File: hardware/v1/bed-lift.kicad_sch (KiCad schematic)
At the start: 69 parts, among them J1 SM04B-SRSS-TB, J2 S2P-VH, J3 SM04B-SRSS-TB, J4 S3B-XH-A, J5 S6B-XH-A, J6 Conn_02x08_Odd_Even, J7 S6B-XH-A, J8 BM04B-SRSS-TB, J9 Conn_ST_STDC14, Q1 MMBT3904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

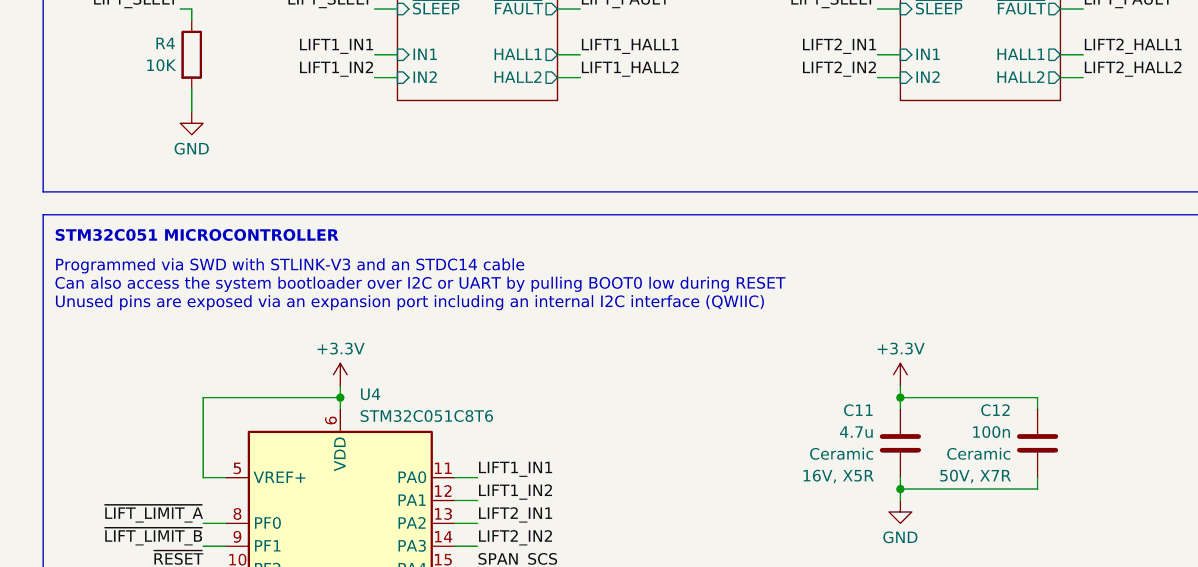
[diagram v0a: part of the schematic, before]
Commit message: Correct the BOOT0 pin polarity in the documentation.
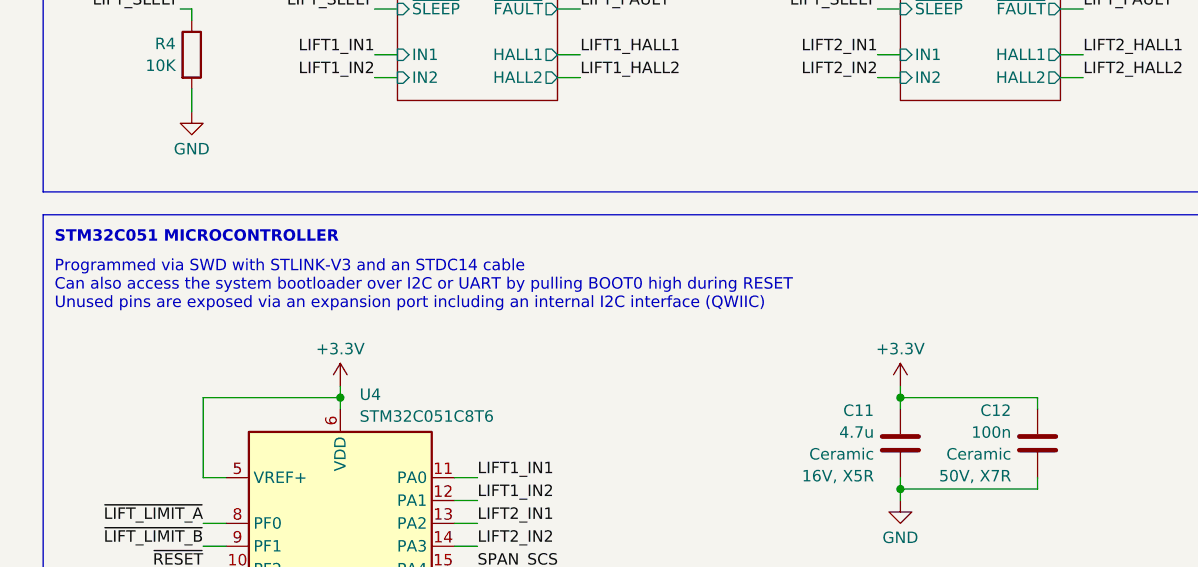
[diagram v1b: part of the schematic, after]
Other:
- note added: "Programmed via SWD with STLINK-V3 and an STDC14 cable Can also access the system bootloader over I2C or UART by pulling BOOT0 high during RESET Unused pins are exposed via an expansion port including an internal I2C interface (QWIIC)"
- note removed: "Programmed via SWD with STLINK-V3 and an STDC14 cable Can also access the system bootloader over I2C or UART by pulling BOOT0 low during RESET Unused pins are exposed via an expansion port including an internal I2C interface (QWIIC)"
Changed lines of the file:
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@@
 		)
 	)
-	(text "Programmed via SWD with STLINK-V3 and an STDC14 cable\nCan also access the system bootloader over I2C or UART by pulling BOOT0 low during RESET\nUnused pins are exposed via an expansion port including an internal I2C interface (QWIIC)"
+	(text "Programmed via SWD with STLINK-V3 and an STDC14 cable\nCan also access the system bootloader over I2C or UART by pulling BOOT0 high during RESET\nUnused pins are exposed via an expansion port including an internal I2C interface (QWIIC)"
 		(exclude_from_sim no)
 		(at 15.24 107.95 0)

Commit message: Finalize for production of v1.0 revision.
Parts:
- BZ1: now fitted; now in the parts list
- C3: Alternative A750KW687M1EAAE016 -> (none); Part Alternative (none) -> A750KW687M1EAAE016
- D1: FT Rotation Offset 180 -> 0
- D2, D3: value PESD5V0S2UAT -> PESD5V0L2UU; footprint Package_TO_SOT_SMD:SOT-23 -> Package_TO_SOT_SMD:SOT-323_SC-70; FT Rotation Offset (none) -> 180; LCSC C552572 -> C78769; LCSC Alternative (none) -> C28646364
- D5: LCSC Alternative (none) -> C456091; LCSC_Alternative C456091 -> (none)
- J1, J3: Alternative GT-A1002WRS-104SBT01 -> (none); LCSC Alternative (none) -> C41431904; LCSC_Alternative C41431904 -> (none); Part Alternative (none) -> GT-A1002WRS-104SBT01
- Q1: LCSC Alternative (none) -> C239187; LCSC_Alternative C239187 -> (none)
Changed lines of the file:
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@@
 		(unit 1)
 		(exclude_from_sim no)
-		(in_bom no)
+		(in_bom yes)
 		(on_board yes)
-		(dnp yes)
+		(dnp no)
 		(fields_autoplaced yes)
 		(property "Reference" "BZ1"
@@
 	)
 	(symbol
+		(lib_id "Device:D_Zener_Dual_CommonAnode_KKA_Parallel")
+		(at 222.25 142.24 0)
+		(mirror y)
+		(unit 1)
+		(exclude_from_sim no)
+		(in_bom yes)
+		(on_board yes)
+		(dnp no)
+		(property "Reference" "D2"
+			(at 229.87 141.0857 0)
+			(effects
+				(font
+					(size 1.27 1.27)
+				)
+				(justify right)
+			)
+		)
+		(property "Value" "PESD5V0L2UU"
+			(at 229.87 143.51 0)
+			(effects
+				(font
+					(size 1.27 1.27)
+				)
+				(justify right)
+			)
+		)
+		(property "Footprint" "Package_TO_SOT_SMD:SOT-323_SC-70"
+			(at 223.52 142.24 0)
+			(effects
+				(font
+					(size 1.27 1.27)
+				)
+				(hide yes)
+			)
+		)
+		(property "Datasheet" "https://assets.nexperia.com/documents/data-sheet/PESD5V0L2UU.pdf"
+			(at 223.52 142.24 0)
+			(effects
+				(font
+					(size 1.27 1.27)
+				)
+				(hide yes)
+			)
+		)
+		(property "Description" "Dual Zener diode, common anode on pin 3"
+			(at 222.25 142.24 0)
+			(effects
+				(font
+					(size 1.27 1.27)
+				)
+				(hide yes)
+			)
+		)
+		(property "LCSC" "C78769"
+			(at 222.25 142.24 0)
+			(effects
+				(font
+					(size 1.27 1.27)
+				)
+				(hide yes)
+			)
+		)
+		(property "LCSC Alternative" "C28646364"
+			(at 222.25 142.24 0)
+			(effects
+				(font
+					(size 1.27 1.27)
+				)
+				(hide yes)
+			)
+		)
+		(property "FT Rotation Offset" "180"
+			(at 222.25 142.24 0)
+			(effects
+				(font
+					(size 1.27 1.27)
+				)
+				(hide yes)
+			)
+		)
+		(pin "2"
+		)
+		(pin "3"
+		)
+		(pin "1"
+		)
+		(instances
+			(project "bed-lift"
+				(path "/e474b45c-bd68-4fa4-b324-364b1493394e"
+					(reference "D2")
+					(unit 1)
+				)
+			)
+		)
+	)
+	(symbol
 		(lib_id "power:+3.3V")
 		(at 109.22 121.92 0)
@@
 			)
 		)
-		(property "LCSC_Alternative" "C456091"
+		(property "LCSC Alternative" "C456091"
 			(at 130.81 260.35 0)
 			(effects
@@
 			)
 		)
-		(property "Alternative" " GT-A1002WRS-104SBT01"
+		(property "LCSC Alternative" "C41431904"
 			(at 266.7 38.1 0)
 			(effects
@@
 			)
 		)
-		(property "LCSC_Alternative" "C41431904"
+		(property "Part Alternative" " GT-A1002WRS-104SBT01"
 			(at 266.7 38.1 0)
 			(effects
@@
 			)
 		)
-		(property "Alternative" "A750KW687M1EAAE016"
-			(at 56.261 49.6796 0)
+		(property "Part Alternative" "A750KW687M1EAAE016"
+			(at 53.34 45.72 0)
 			(effects
 				(font
 					(size 1.27 1.27)
 				)
-				(justify left)
 				(hide yes)
 			)
@@
 	)
 	(symbol
+		(lib_id "Device:D_Zener_Dual_CommonAnode_KKA_Parallel")
+		(at 222.25 207.01 0)
+		(mirror y)
+		(unit 1)
+		(exclude_from_sim no)
+		(in_bom yes)
+		(on_board yes)
+		(dnp no)
+		(property "Reference" "D3"
+			(at 229.87 205.8557 0)
+			(effects
+				(font
+					(size 1.27 1.27)
+				)
+				(justify right)
+			)
+		)
+		(property "Value" "PESD5V0L2UU"
+			(at 229.87 208.28 0)
+			(effects
+				(font
+					(size 1.27 1.27)
+				)
+				(justify right)
+			)
+		)
+		(property "Footprint" "Package_TO_SOT_SMD:SOT-323_SC-70"
+			(at 223.52 207.01 0)
+			(effects
+				(font
+					(size 1.27 1.27)
+				)
+				(hide yes)
+			)
+		)
+		(property "Datasheet" "https://assets.nexperia.com/documents/data-sheet/PESD5V0L2UU.pdf"
+			(at 223.52 207.01 0)
+			(effects
+				(font
+					(size 1.27 1.27)
+				)
+				(hide yes)
+			)
+		)
+		(property "Description" "Dual Zener diode, common anode on pin 3"
+			(at 222.25 207.01 0)
+			(effects
+				(font
+					(size 1.27 1.27)
+				)
+				(hide yes)
+			)
+		)
+		(property "LCSC" "C78769"
+			(at 222.25 207.01 0)
+			(effects
+				(font
+					(size 1.27 1.27)
+				)
+				(hide yes)
+			)
+		)
+		(property "LCSC Alternative" "C28646364"
+			(at 222.25 207.01 0)
+			(effects
+				(font
+					(size 1.27 1.27)
+				)
+				(hide yes)
+			)
+		)
+		(property "FT Rotation Offset" "180"
+			(at 222.25 207.01 0)
+			(effects
+				(font
+					(size 1.27 1.27)
+				)
+				(hide yes)
+			)
+		)
+		(pin "2"
+		)
+		(pin "3"
+		)
+		(pin "1"
+		)
+		(instances
+			(project "bed-lift"
+				(path "/e474b45c-bd68-4fa4-b324-364b1493394e"
+					(reference "D3")
+					(unit 1)
+				)
+			)
+		)
+	)
+	(symbol
 		(lib_id "Device:R")
 		(at 284.48 137.16 90)
@@
 			)
 		)
-		(property "LCSC_Alternative" "C456091"
+		(property "LCSC Alternative" "C456091"
 			(at 130.81 240.03 0)
 			(effects
@@
 			)
 		)
-		(property "LCSC_Alternative" "C239187"
+		(property "LCSC Alternative" "C239187"
 			(at 281.94 194.31 0)
 			(effects
@@
 			)
 		)
-		(property "LCSC_Alternative" "C456091"
+		(property "LCSC Alternative" "C456091"
 			(at 130.81 250.19 0)
 			(effects
@@
 	)
 	(symbol
-		(lib_id "Device:D_Zener_Dual_CommonAnode_KKA_Parallel")
-		(at 222.25 207.01 0)
-		(mirror y)
-		(unit 1)
-		(exclude_from_sim no)
-		(in_bom yes)
-		(on_board yes)
-		(dnp no)
-		(property "Reference" "D3"
-			(at 229.87 205.74 0)
-			(effects
-				(font
-					(size 1.27 1.27)
-				)
-				(justify right)
-			)
-		)
-		(property "Value" "PESD5V0S2UAT"
-			(at 229.87 208.28 0)
-			(effects
-				(font
-					(size 1.27 1.27)
-				)
-				(justify right)
-			)
-		)
-		(property "Footprint" "Package_TO_SOT_SMD:SOT-23"
-			(at 223.52 207.01 0)
-			(effects
-				(font
-					(size 1.27 1.27)
-				)
-				(hide yes)
-			)
-		)
-		(property "Datasheet" "https://assets.nexperia.com/documents/data-sheet/PESD5V0S2UAT.pdf"
-			(at 223.52 207.01 0)
-			(effects
-				(font
-					(size 1.27 1.27)
-				)
-				(hide yes)
-			)
-		)
-		(property "Description" "Dual Zener diode, common anode on pin 3"
-			(at 222.25 207.01 0)
-			(effects
-				(font
-					(size 1.27 1.27)
-				)
-				(hide yes)
-			)
-		)
-		(property "LCSC" "C552572"
-			(at 222.25 207.01 0)
-			(effects
-				(font
-					(size 1.27 1.27)
-				)
-				(hide yes)
-			)
-		)
-		(pin "2"
-		)
-		(pin "3"
-		)
-		(pin "1"
-		)
-		(instances
-			(project "bed-lift"
-				(path "/e474b45c-bd68-4fa4-b324-364b1493394e"
-					(reference "D3")
-					(unit 1)
-				)
-			)
-		)
-	)
-	(symbol
 		(lib_id "power:GND")
 		(at 342.9 57.15 0)
@@
 			)
 		)
-		(property "Alternative" " GT-A1002WRS-104SBT01"
+		(property "LCSC Alternative" "C41431904"
 			(at 266.7 57.15 0)
 			(effects
@@
 			)
 		)
-		(property "LCSC_Alternative" "C41431904"
+		(property "Part Alternative" " GT-A1002WRS-104SBT01"
 			(at 266.7 57.15 0)
 			(effects
@@
 			)
 		)
-		(property "FT Rotation Offset" "180"
+		(property "FT Rotation Offset" "0"
 			(at 39.37 45.72 90)
 			(effects
@@
 			)
 		)
-		(property "LCSC_Alternative" "C456091"
+		(property "LCSC Alternative" "C456091"
 			(at 130.81 255.27 0)
 			(effects
@@
 			)
 		)
-		(property "LCSC_Alternative" "C456091"
+		(property "LCSC Alternative" "C456091"
 			(at 130.81 245.11 0)
 			(effects
@@
 					(unit 1)
 				)
-			)
-		)
-	)
-	(symbol
-		(lib_id "Device:D_Zener_Dual_CommonAnode_KKA_Parallel")
-		(at 222.25 142.24 0)
-		(mirror y)
-		(unit 1)
-		(exclude_from_sim no)
-		(in_bom yes)
-		(on_board yes)
-		(dnp no)
-		(fields_autoplaced yes)
-		(property "Reference" "D2"
-			(at 229.87 140.97 0)
-			(effects
-				(font
-					(size 1.27 1.27)
-				)
-				(justify right)
-			)
-		)
-		(property "Value" "PESD5V0S2UAT"
-			(at 229.87 143.51 0)
-			(effects
-				(font
-					(size 1.27 1.27)
-				)
-				(justify right)
-			)
-		)
-		(property "Footprint" "Package_TO_SOT_SMD:SOT-23"
-			(at 223.52 142.24 0)
-			(effects
-				(font
-					(size 1.27 1.27)
-				)
-				(hide yes)
-			)
-		)
-		(property "Datasheet" "https://assets.nexperia.com/documents/data-sheet/PESD5V0S2UAT.pdf"
-			(at 223.52 142.24 0)
-			(effects
-				(font
-					(size 1.27 1.27)
-				)
-				(hide yes)
-			)
-		)
-		(property "Description" "Dual Zener diode, common anode on pin 3"
-			(at 222.25 142.24 0)
-			(effects
-				(font
-					(size 1.27 1.27)
-				)
-				(hide yes)
-			)
-		)
-		(property "LCSC" "C552572"
-			(at 222.25 142.24 0)
-			(effects
-				(font
-					(size 1.27 1.27)
-				)
-				(hide yes)
-			)
-		)
-		(pin "2"
-		)
-		(pin "3"
-		)
-		(pin "1"
-		)
-		(instances
-			(project "bed-lift"
-				(path "/e474b45c-bd68-4fa4-b324-364b1493394e"
-					(reference "D2")
-					(unit 1)
-				)
